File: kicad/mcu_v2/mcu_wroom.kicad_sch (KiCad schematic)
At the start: 20 parts, among them J141 TYPE-C-31-M-12, SW141 RESET, SW142 BOOT, U105 ESP32-S3-WROOM-1-N16R8, U141 AMS1117-3.3, U142 USBLC6-2SC6

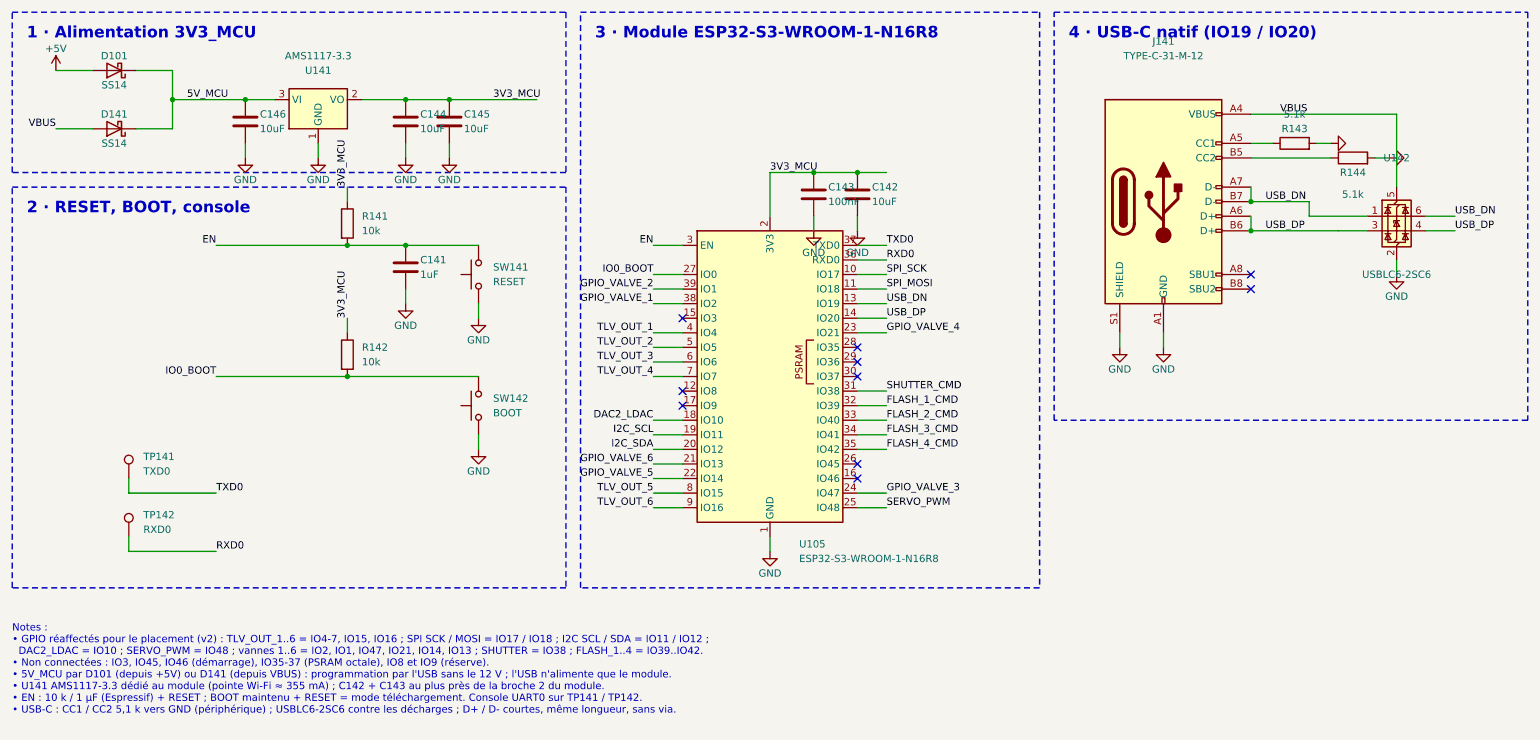
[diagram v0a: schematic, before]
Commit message: Feuille MCU v2 : ajout des tirages I2C R108 / R109 (4,7 k vers +3V3), netlist revérifiée (37 nets, 0 écart)
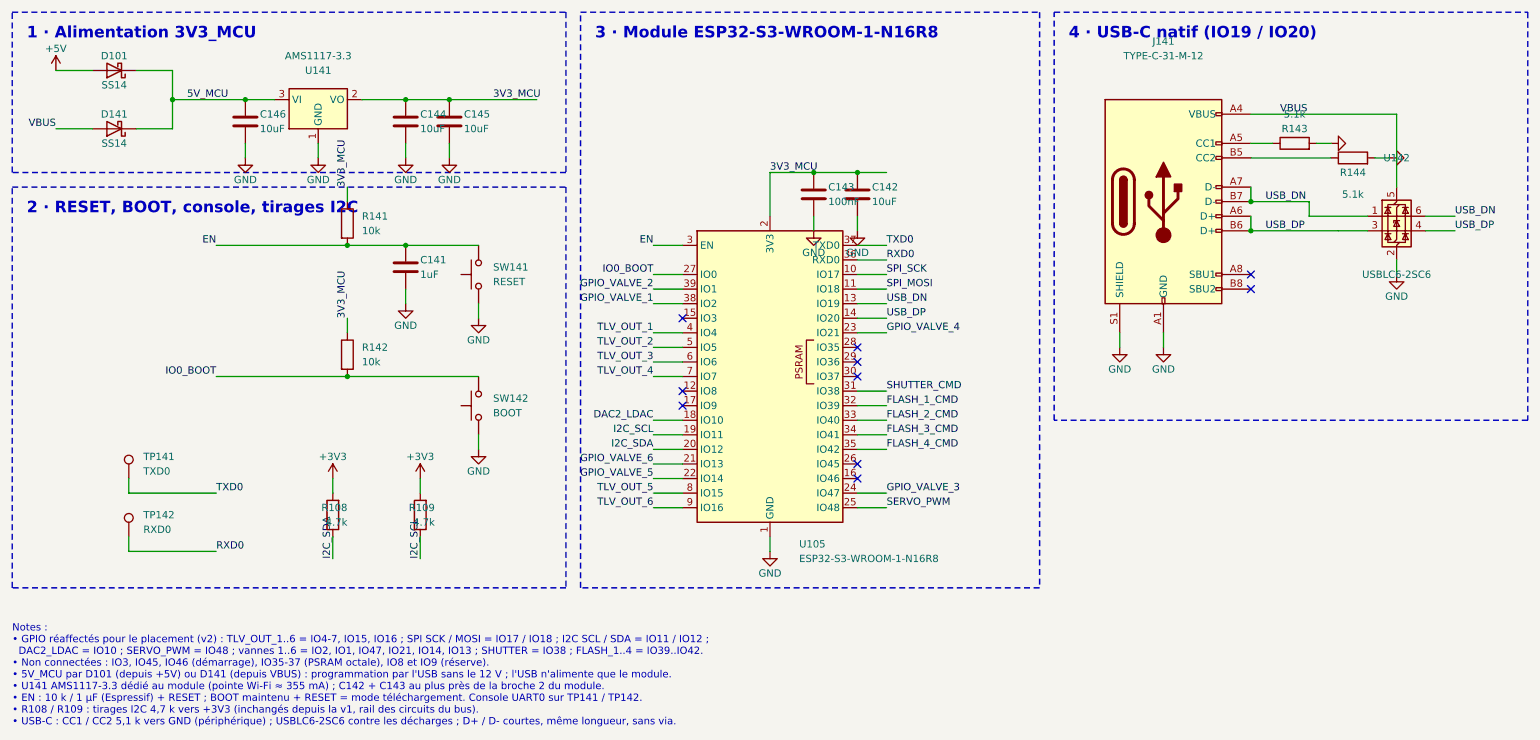
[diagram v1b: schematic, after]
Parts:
- added R143, R144: 5.1k, symbol Device:R
- J141: renamed from R144; value 5.1k -> TYPE-C-31-M-12; symbol Device:R -> Connector:USB_C_Receptacle_USB2.0_16P; LCSC C23186 -> C165948
- R108: renamed from J141; value TYPE-C-31-M-12 -> 4.7k; symbol Connector:USB_C_Receptacle_USB2.0_16P -> Device:R; LCSC C165948 -> C23162
- R109: renamed from R143; value 5.1k -> 4.7k; LCSC C23186 -> C23162
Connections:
- net GND: now also J141.A1 (GND), J141.A12 (GND), J141.B1 (GND), J141.B12 (GND), J141.S1 (SHIELD), R143.2, R144.2; no longer J141.2, R108.A1 (GND), R108.A12 (GND), R108.B1 (GND), R108.B12 (GND), R108.S1 (SHIELD), R109.2
- net I2C_SCL: now also R109.1
- net I2C_SDA: now also R108.1
- net USB_DN: now also J141.A7 (D-), J141.B7 (D-); no longer R108.A7 (D-), R108.B7 (D-)
- net USB_DP: now also J141.A6 (D+), J141.B6 (D+); no longer R108.A6 (D+), R108.B6 (D+)
- net VBUS: now also J141.A4 (VBUS), J141.A9 (VBUS), J141.B4 (VBUS), J141.B9 (VBUS); no longer R108.A4 (VBUS), R108.A9 (VBUS), R108.B4 (VBUS), R108.B9 (VBUS)
- new net: J141.B5 (CC2), R144.1
- new net: J141.A5 (CC1), R143.1
- new net +3V3: R108.2, R109.2
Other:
- note added: "2 · RESET, BOOT, console, tirages I2C"
- note removed: "2 · RESET, BOOT, console"
- moved on the sheet: R109
